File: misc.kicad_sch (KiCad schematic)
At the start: 26 parts, among them J3 PinSocket_2x11_P2.54mm_Drill1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, U2 NTS0102_TSSOP, U3 NTS0102_TSSOP, Y1 Oscillator_25MHz_511ABA25M000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, Y2 Resonator_50MHz_XRCGE

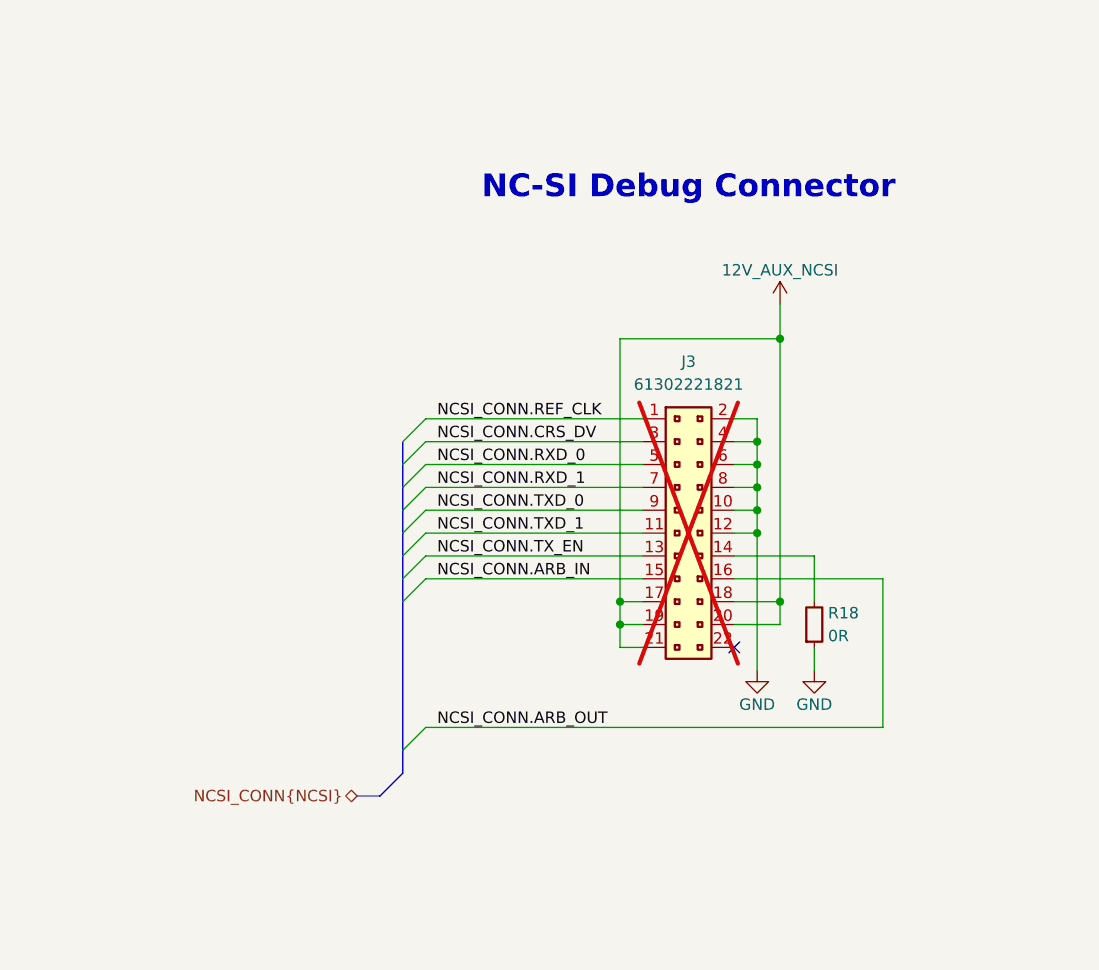
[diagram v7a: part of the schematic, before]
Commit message: [#80813] Change PCB mounts, replace NCSI connector with testpoints
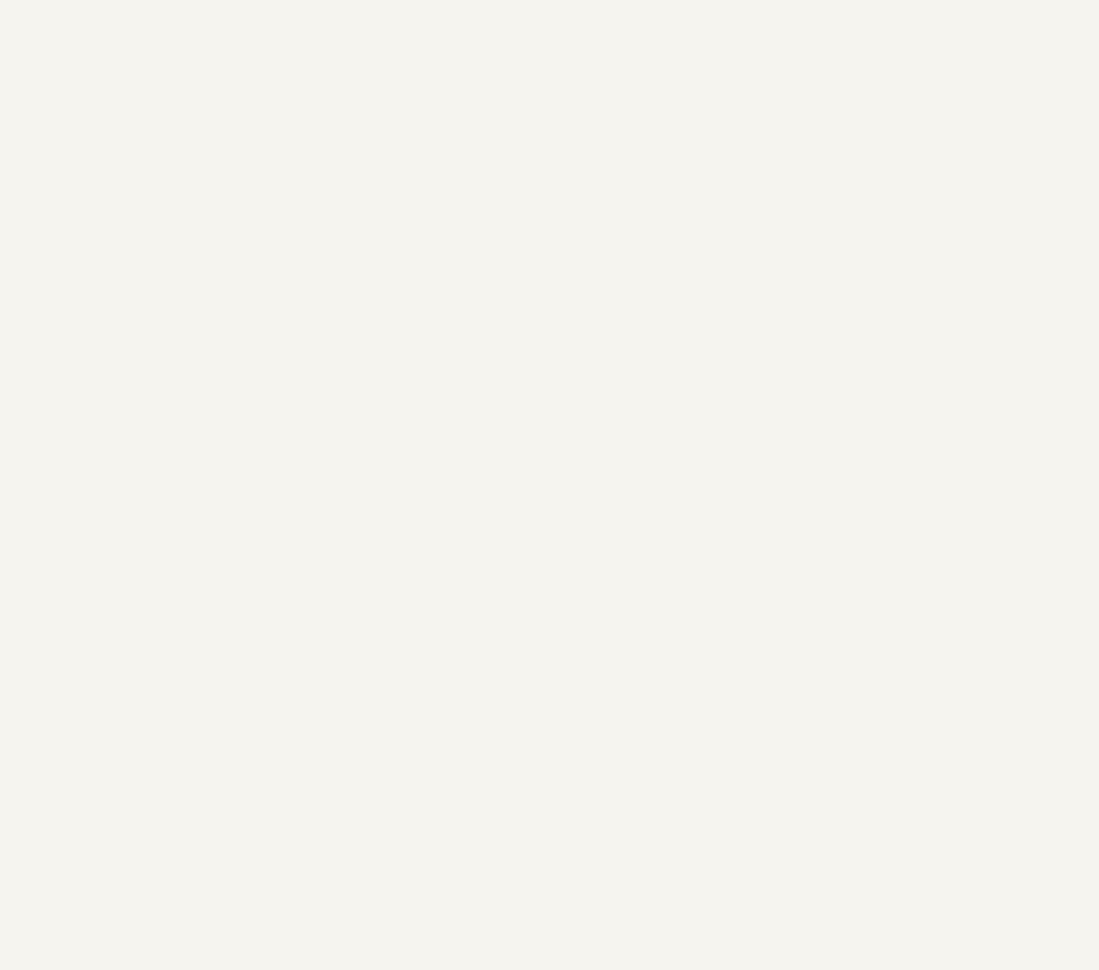
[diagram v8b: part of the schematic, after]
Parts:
- removed J3: PinSocket_2x11_P2.54mm_Drill1.02mm, antmicro-footprints:PinSocket_2x11_P2.54mm_Drill1.02mm, symbol antmicroGenericPinSockets:PinSocket_2x11_P2.54mm_Drill1.02mm
- removed R18: R_0R_0402, antmicro-footprints:R_0402_1005Metric, symbol antmicroResistors0402:R_0R_0402
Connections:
- no-connect marks 1 -> 0
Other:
- note removed: "NC-SI Debug Connector"
